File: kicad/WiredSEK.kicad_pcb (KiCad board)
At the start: 4 copper layers, 50.2 x 37.7 mm, 51 parts, among them J1 Conn_01x34, J2 USB_C_Receptacle, J3 AVR-JTAG-10, J4 Serial RX/TX, J5 Testpad, SW1 HWB_SW, SW2 RST_SW, U1 USBLC6-2SC6, U2 AT90USB646-AU, Y1 16 Mhz

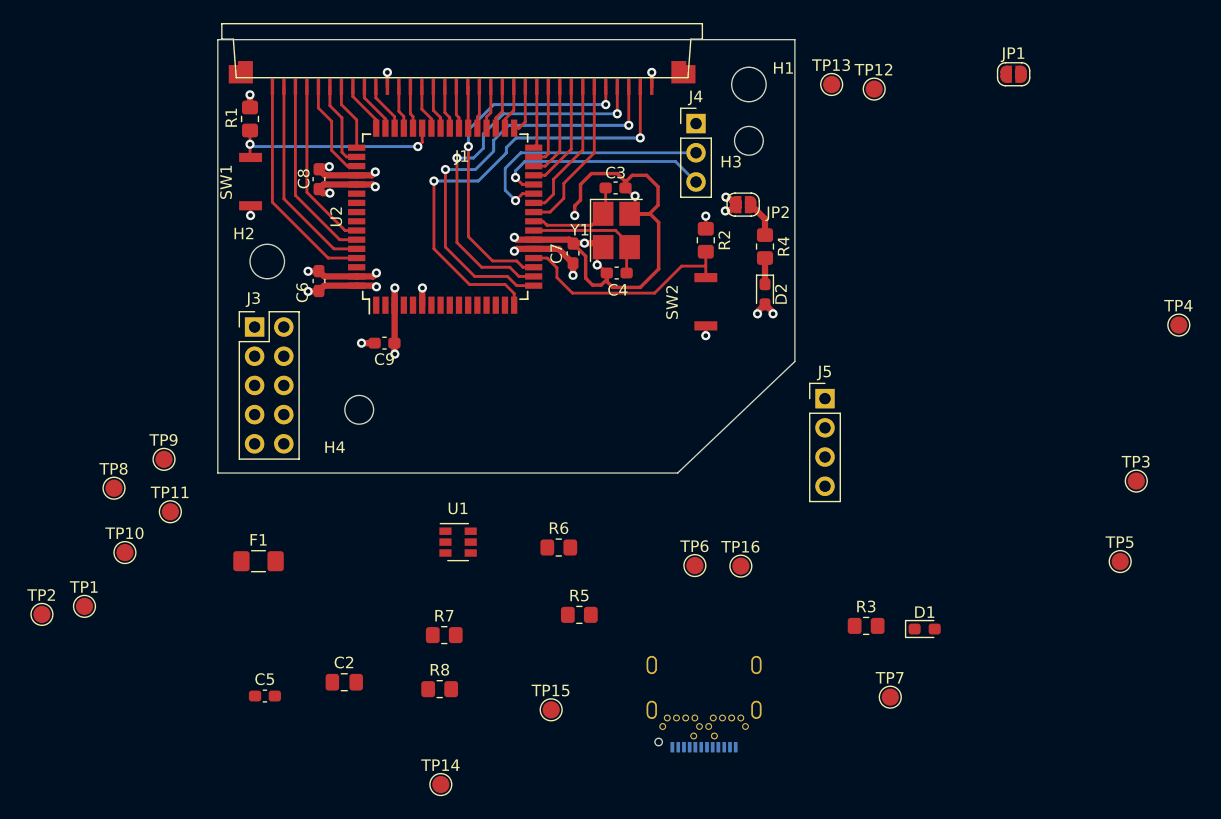
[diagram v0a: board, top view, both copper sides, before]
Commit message: done with pcb routing
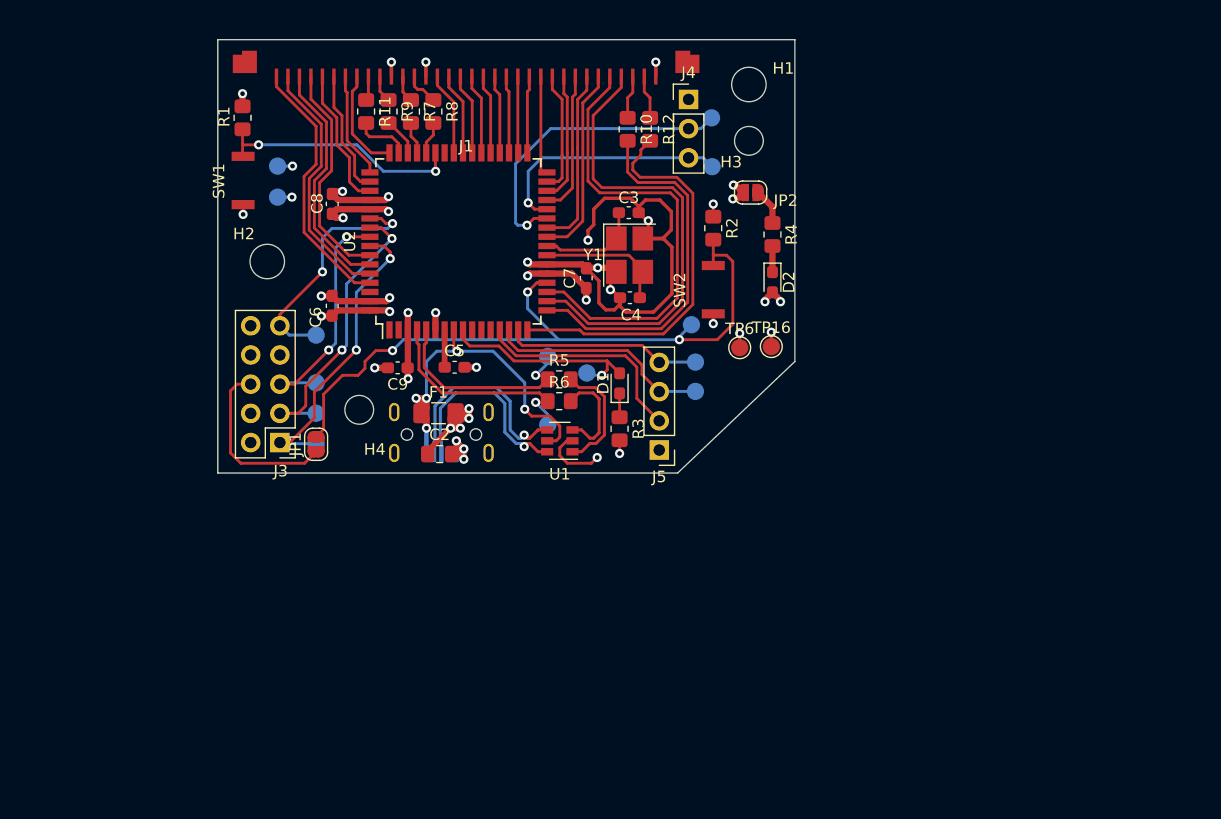
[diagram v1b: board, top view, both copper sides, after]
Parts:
- added R10: 2k, Resistor_SMD:R_0805_2012Metric_Pad1.20x1.40mm_HandSolder, F.Cu at (103.7, 48.8)
- added R11: 2k, Resistor_SMD:R_0805_2012Metric_Pad1.20x1.40mm_HandSolder, F.Cu at (80.9, 47.2)
- added R12: 2k, Resistor_SMD:R_0805_2012Metric_Pad1.20x1.40mm_HandSolder, F.Cu at (105.6, 48.8)
- added R9: 2k, Resistor_SMD:R_0805_2012Metric_Pad1.20x1.40mm_HandSolder, F.Cu at (82.8, 47.2)
- J2: value USB_C_Receptacle -> USB_B_Micro; footprint WiredSEK:SJ121226 -> WiredSEK:GMCB05801124EU
- R7, R8: value 5k1 -> ??
- TP1, TP10, TP11, TP12, TP13, TP14, TP15, TP2, TP3, TP4, TP5, TP7, TP8, TP9: moved to B.Cu
- moved JP1 68.7 mm to (76.5, 76.2), turned to 90 degrees
- moved R8 50.3 mm to (86.8, 47.2), turned to 270 degrees
- moved R7 45.6 mm to (84.8, 47.2), turned to 270 degrees
- moved TP4 42.2 mm to (109.5, 69.0)
- moved TP1 41.8 mm to (73.2, 52.0)
- moved TP2 41.7 mm to (73.2, 54.7)
- moved TP3 41.0 mm to (109.2, 65.8)
- moved TP5 39.8 mm to (109.5, 71.6)
- moved TP7 38.6 mm to (100.1, 70.0)
- moved TP14 38.4 mm to (96.7, 68.5)
- moved J2 35.2 mm to (87.5, 75.3)
- moved D1 34.1 mm to (103.0, 70.9), turned to 90 degrees
- moved C5 33.0 mm to (88.6, 69.5)
- moved R3 27.5 mm to (103.0, 74.8), turned to 270 degrees
- moved TP15 24.8 mm to (96.7, 74.5)
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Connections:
- net KCON_1 renamed KROW_0
- net KCON_15 renamed KCOL_0
- net KCON_16 renamed KCOL_1
- net KCON_17 renamed KCOL_2
- net KCON_18 renamed KCOL_3
- net KCON_19 renamed KCOL_4
- net KCON_2 renamed KROW_1
- net KCON_20 renamed KCOL_5
- net KCON_21 renamed KCOL_6
- net KCON_22 renamed KCOL_7
- net KCON_23 renamed KCOL_8
- net KCON_24 renamed KCOL_9
- net KCON_25 renamed KCOL_10
- net KCON_26 renamed KCOL_11
- net KCON_27 renamed KCOL_12
- net KCON_28 renamed KCOL_13
- net KCON_29 renamed KCOL_14
- net KCON_3 renamed KROW_2
- net KCON_30 renamed KCOL_15
- net KCON_31 renamed KCOL_16
- net KCON_4 renamed KROW_3
- net KCON_5 renamed KROW_4
- net KCON_6 renamed KROW_5
- net KCON_7 renamed KROW_6
- net KCON_8 renamed KROW_7
- J1 pad 10: KCON_10 -> Net-(J1-Pad10)
- J1 pad 12: KCON_12 -> Net-(J1-Pad12)
- J1 pad 13: KCON_13 -> Net-(J1-Pad13)
- J1 pad 14: KCON_14 -> +5V
- J1 pad 32: KCON_32 -> Net-(J1-Pad32)
- J1 pad 33: KCON_33 -> Net-(J1-Pad33)
- J1 pad 9: KCON_9 -> Net-(J1-Pad9)
- R7 pad 1: CC1 -> Net-(J1-Pad12)
- R7 pad 2: GND -> PRW_LED
- R8 pad 1: CC2 -> Net-(J1-Pad13)
- R8 pad 2: GND -> PRR_LED
- U2 pad 16: KCON_33 -> RL_LED
- U2 pad 17: KCON_32 -> FN_LED
- U2 pad 42: KCON_14 -> (no net)
- U2 pad 44: KCON_13 -> PRR_LED
- U2 pad 45: KCON_12 -> PRW_LED
- U2 pad 46: KCON_10 -> CL_LED
- U2 pad 47: KCON_9 -> NL_LED
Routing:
- net RESET: track 20.0 -> 61.1 mm, vias 0 -> 3
- net KCON_33: track 39.7 -> 0.00 mm, vias 2 -> 0
- net KCON_32: track 37.3 -> 0.00 mm, vias 2 -> 0
- net VBUS: track 0.00 -> 34.6 mm, vias 0 -> 5
- net RL_LED: track 0.00 -> 34.5 mm
- net FN_LED: track 0.00 -> 31.9 mm
- net TCK: track 0.00 -> 26.2 mm, vias 0 -> 2
- net TDO: track 0.00 -> 25.6 mm, vias 0 -> 2
- net TDI: track 0.00 -> 21.4 mm, vias 0 -> 2
- net TMS: track 0.00 -> 21.2 mm, vias 0 -> 2
- net GND: track 72.1 -> 92.0 mm, vias 17 -> 25
- net T1: track 0.00 -> 19.5 mm
- net D-: track 0.00 -> 19.4 mm, vias 0 -> 1
- net T2: track 0.00 -> 19.2 mm
- net LED_STATUS: track 0.00 -> 18.5 mm, vias 0 -> 1
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
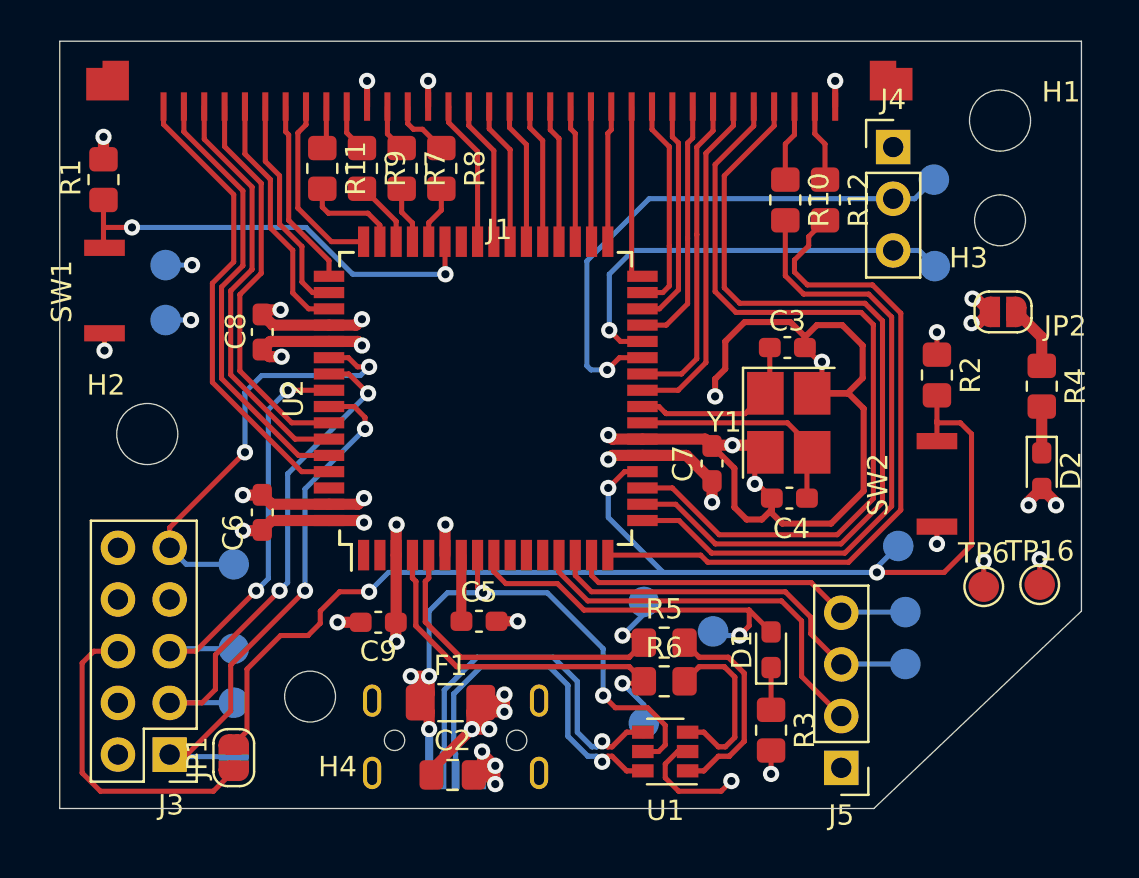
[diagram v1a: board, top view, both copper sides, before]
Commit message: Fixed SW1 and SW2 footprints and cleaned silk layers
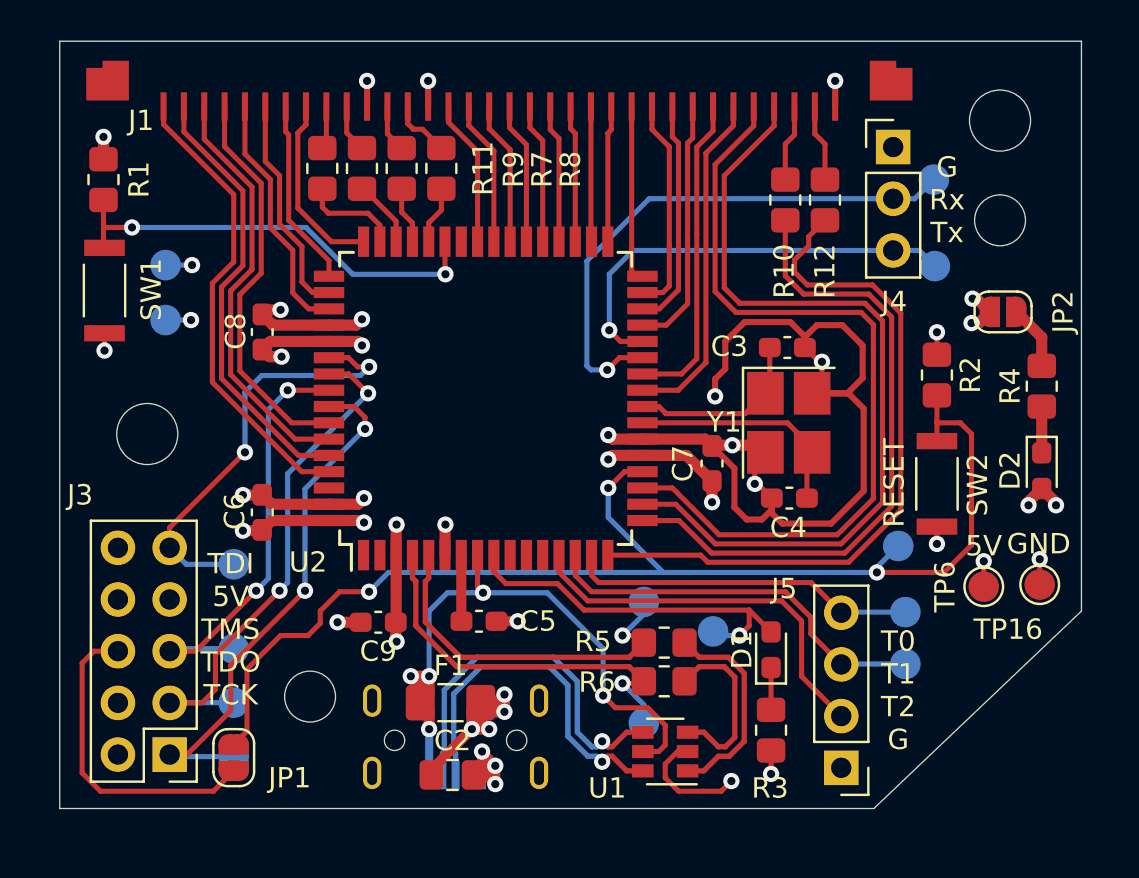
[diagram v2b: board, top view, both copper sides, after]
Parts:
- added REF**: OSHW-Logo2_7.3x6mm_SilkScreen, Symbol:OSHW-Logo2_7.3x6mm_SilkScreen, B.Cu at (76.8, 44.8)
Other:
- board text added: "5V"
- board text added: "D+"
- board text added: "D-"
- board text added: "G Rx Tx"
- board text added: "GND"
- board text added: "LS"
- board text added: "RESET"
- board text added: "RST"
- board text added: "Rx"
- board text added: "T0"
- board text added: "T0 T1 T2 G"
- board text added: "T1"
- board text added: "TCK"
- board text added: "TDI"
- board text added: "TDI 5V TMS TDO TCK"
- board text added: "TDO"
- board text added: "TMS"
- board text added: "Tx"
- board text added: "wiredSEK | Rev 1"

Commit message: preparing for jlcpcb order
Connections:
- J2 pad 4: (no net) -> Net-(J2-Pad4)
- J3 pad 8: (no net) -> Net-(J3-Pad8)
- U2 pad 1: (no net) -> Net-(U2-Pad1)
- U2 pad 10: (no net) -> Net-(U2-Pad10)
- U2 pad 11: (no net) -> Net-(U2-Pad11)
- U2 pad 12: (no net) -> Net-(U2-Pad12)
- U2 pad 2: (no net) -> Net-(U2-Pad2)
- U2 pad 42: (no net) -> Net-(U2-Pad42)
- U2 pad 62: (no net) -> Net-(U2-Pad62)
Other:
- outline, holes or cut-outs redrawn
- board text added: "JLCJLCJLCJLC"

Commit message: added pin 1 and polarity markers
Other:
- board text added: "+"
